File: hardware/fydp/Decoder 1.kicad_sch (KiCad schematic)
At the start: 21 parts, among them J2 Conn_01x02_Pin, J3 Conn_01x02_Pin, J6 Conn_01x04_Pin, U62 74HC139N

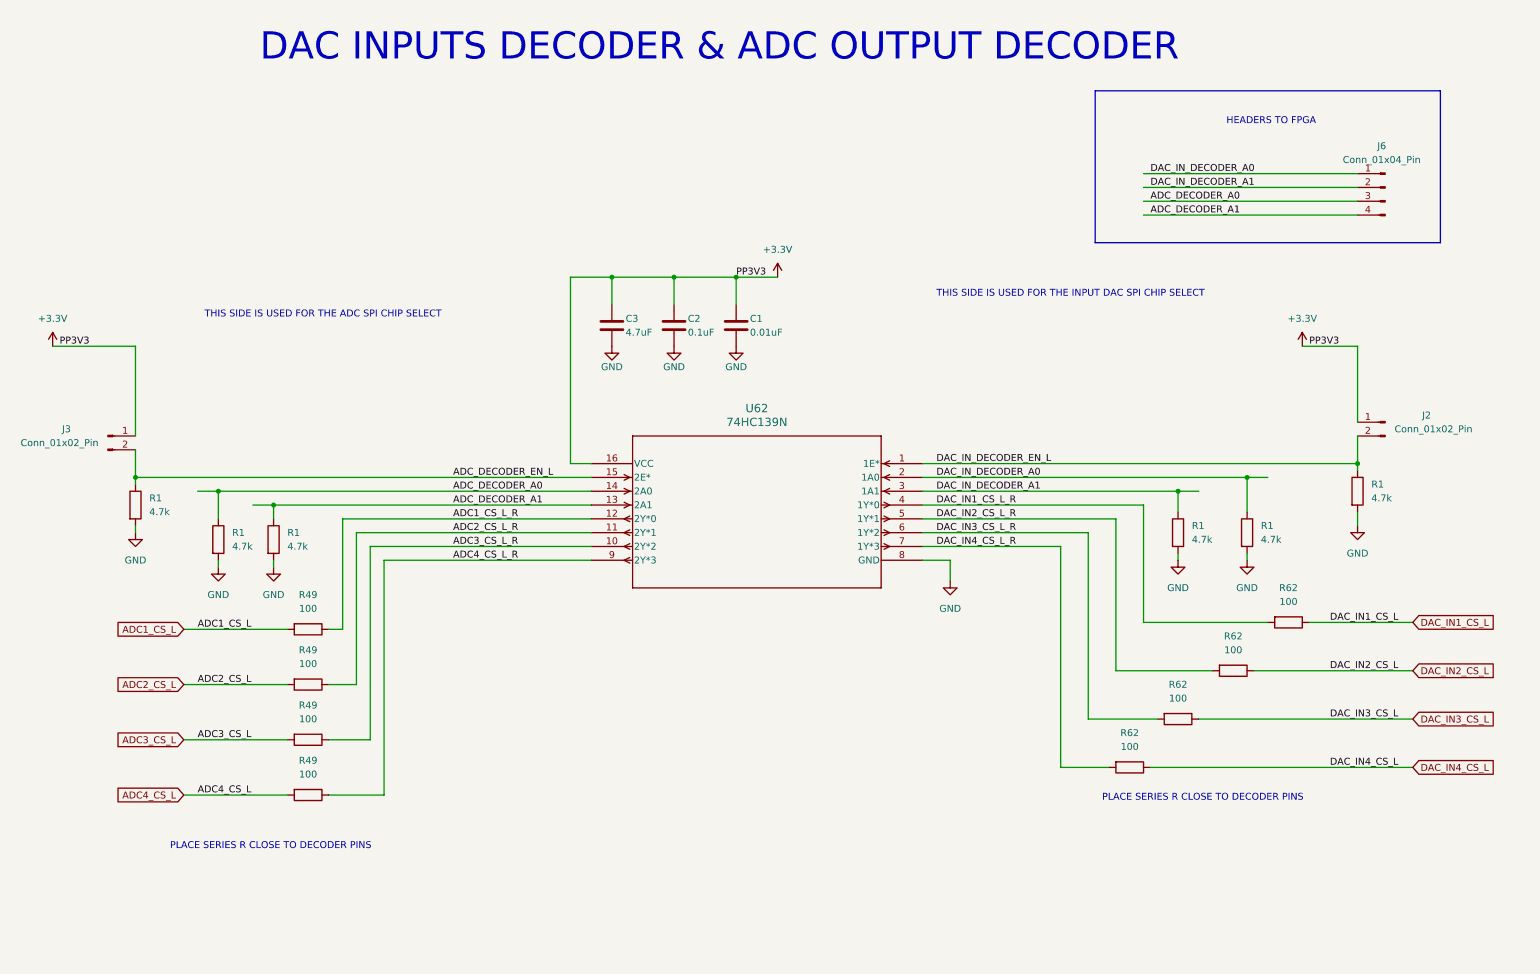
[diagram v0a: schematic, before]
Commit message: Remove 2 channels of multiplier and change ADC
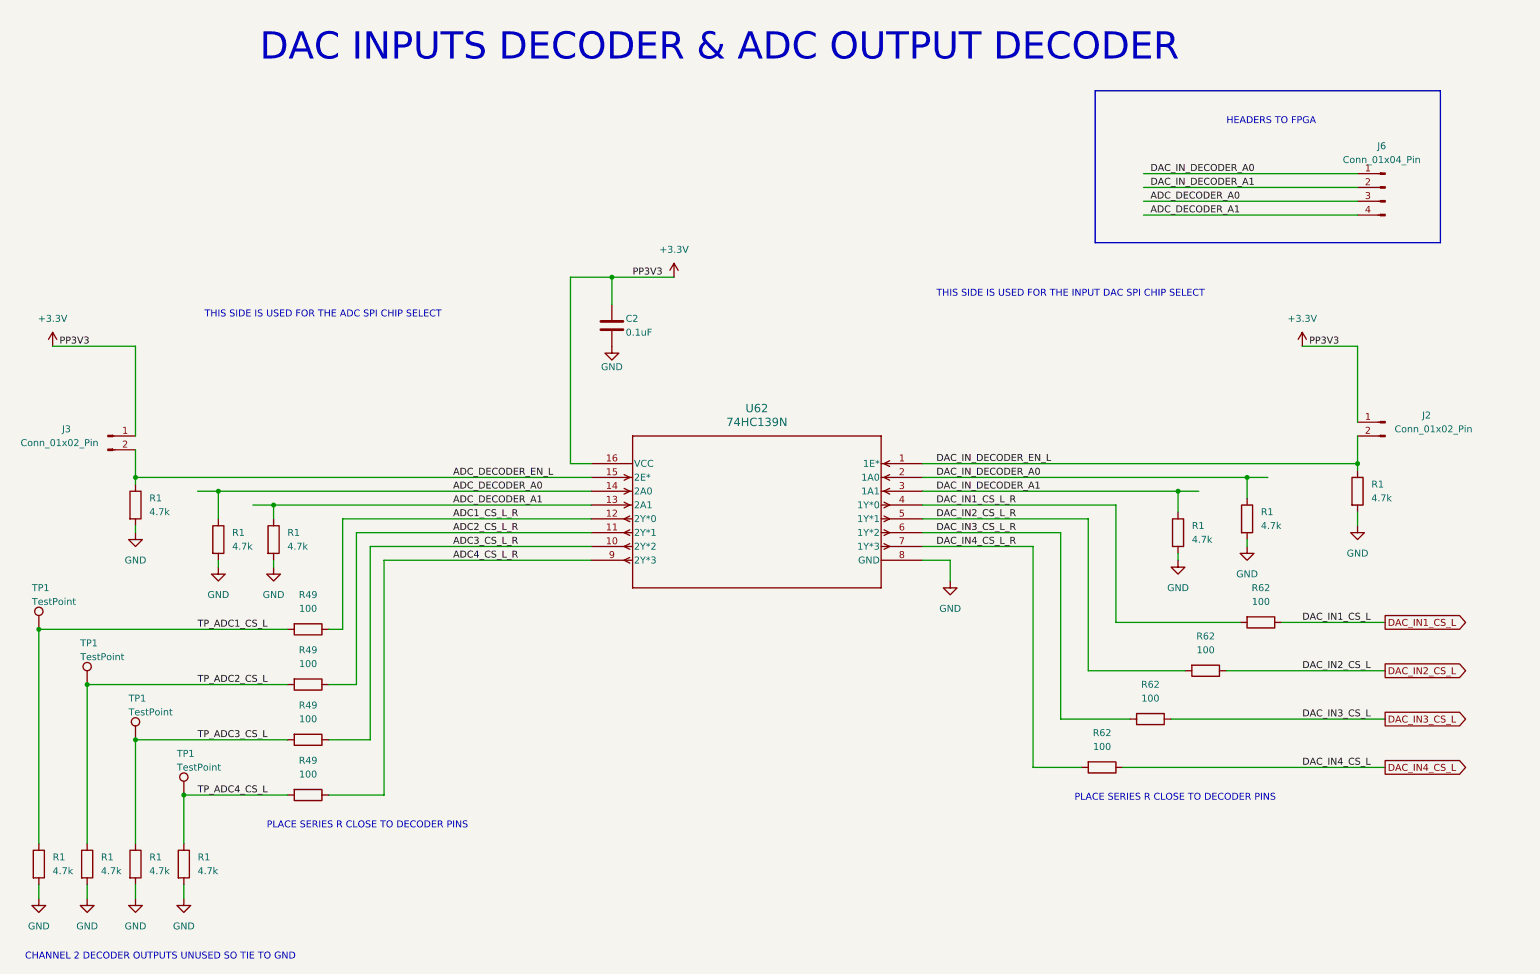
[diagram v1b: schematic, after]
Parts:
- removed C1: 0.01uF, Capacitor_SMD:C_0805_2012Metric, symbol Device:C
- removed C3: 4.7uF, Capacitor_SMD:C_0805_2012Metric, symbol Device:C
- added R1 (x4): 4.7k, Resistor_SMD:R_0805_2012Metric, symbol Device:R
- added TP1 (x4): TestPoint, TestPoint:TestPoint_Pad_1.0x1.0mm, symbol Connector:TestPoint
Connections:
- net GND: now also R1.2, R1.2, R1.2, R1.2
- net ADC1_CS_L renamed TP_ADC1_CS_L
- net TP_ADC1_CS_L: now also R1.1, TP1.1
- net ADC2_CS_L renamed TP_ADC2_CS_L
- net TP_ADC2_CS_L: now also R1.1, TP1.1
- net ADC3_CS_L renamed TP_ADC3_CS_L
- net TP_ADC3_CS_L: now also R1.1, TP1.1
- net ADC4_CS_L renamed TP_ADC4_CS_L
- net TP_ADC4_CS_L: now also R1.1, TP1.1
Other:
- note added: "CHANNEL 2 DECODER OUTPUTS UNUSED SO TIE TO GND"
- moved on the sheet: C2, R1, R62

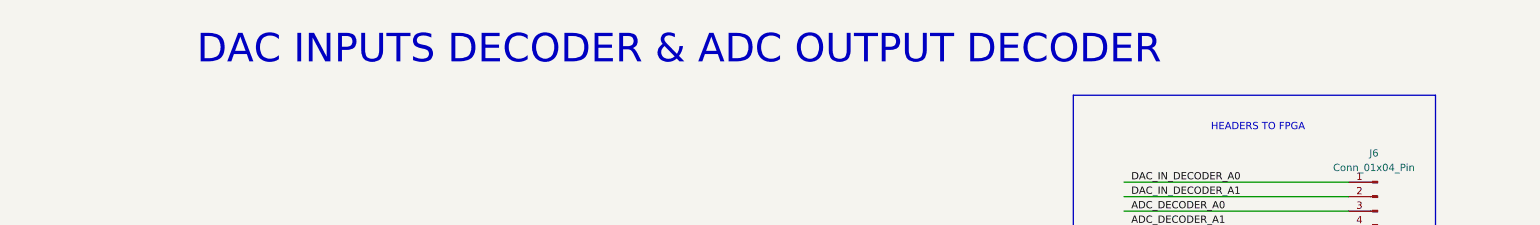
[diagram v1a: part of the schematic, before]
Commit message: Edit schematic titles
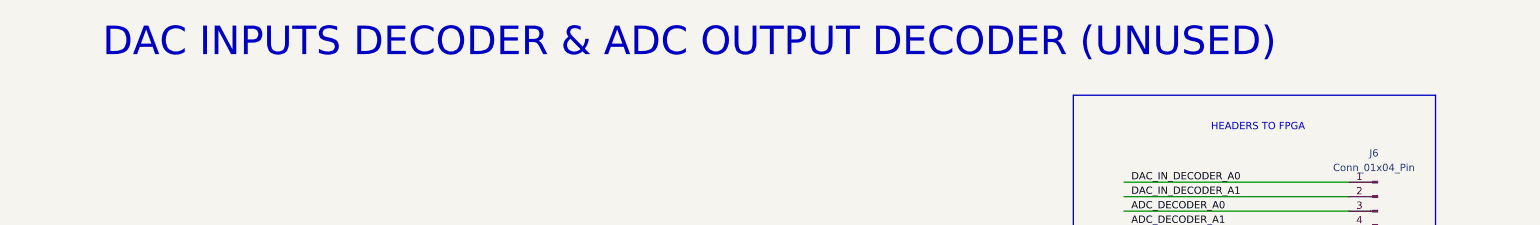
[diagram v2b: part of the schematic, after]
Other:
- note added: "DAC INPUTS DECODER & ADC OUTPUT DECODER (UNUSED)"
- note removed: "DAC INPUTS DECODER & ADC OUTPUT DECODER"
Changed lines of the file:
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@@
     (effects (font (size 1.27 1.27)) (justify left bottom))
   )
-  (text "DAC INPUTS DECODER & ADC OUTPUT DECODER" (at 59.69 26.67 0)
+  (text "DAC INPUTS DECODER & ADC OUTPUT DECODER (UNUSED)" (at 43.18 25.4 0)
     (effects (font (size 5 5)) (justify left bottom))
   )

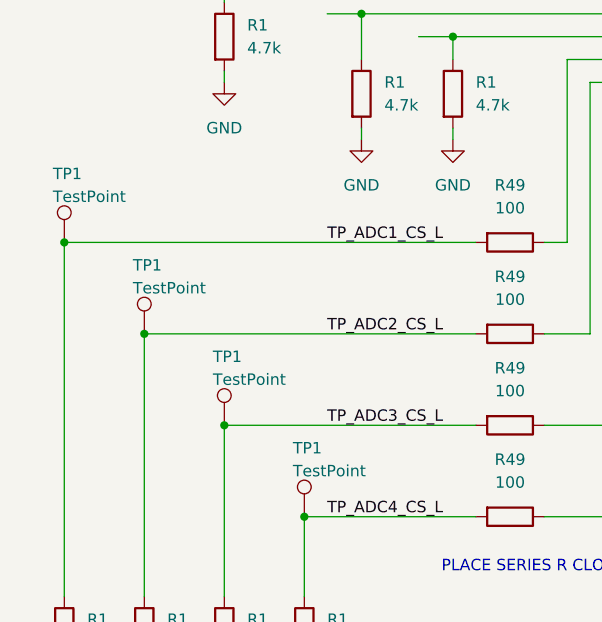
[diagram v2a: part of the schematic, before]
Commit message: Initial layout mostly complete, need to complete lots of routing
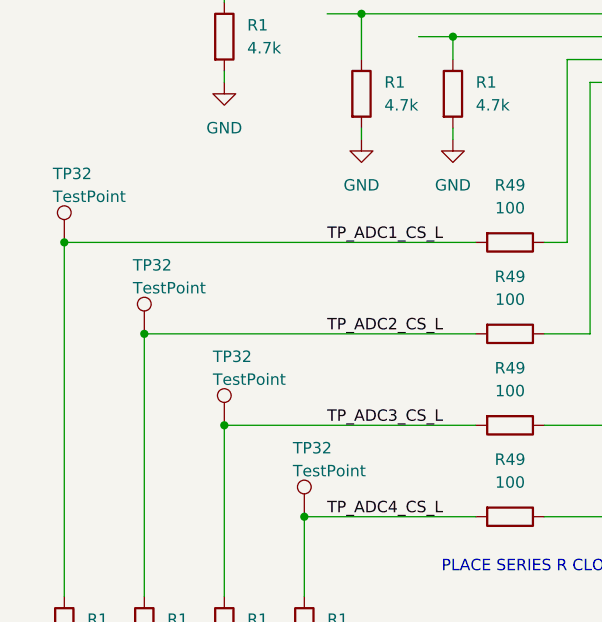
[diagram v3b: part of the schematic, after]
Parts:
- renumbered TP1 to TP32
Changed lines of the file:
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@@
   (symbol (lib_id "Connector:TestPoint") (at 27.94 140.97 0) (unit 1)
     (in_bom yes) (on_board yes) (dnp no)
-    (property "Reference" "TP1" (at 26.67 133.35 0)
+    (property "Reference" "TP32" (at 26.67 133.35 0)
       (effects (font (size 1.27 1.27)) (justify left))
     )
@@
   (symbol (lib_id "Connector:TestPoint") (at 36.83 151.13 0) (unit 1)
     (in_bom yes) (on_board yes) (dnp no)
-    (property "Reference" "TP1" (at 35.56 143.51 0)
+    (property "Reference" "TP32" (at 35.56 143.51 0)
       (effects (font (size 1.27 1.27)) (justify left))
     )
@@
   (symbol (lib_id "Connector:TestPoint") (at 45.72 161.29 0) (unit 1)
     (in_bom yes) (on_board yes) (dnp no)
-    (property "Reference" "TP1" (at 44.45 153.67 0)
+    (property "Reference" "TP32" (at 44.45 153.67 0)
       (effects (font (size 1.27 1.27)) (justify left))
     )
@@
   (symbol (lib_id "Connector:TestPoint") (at 19.05 130.81 0) (unit 1)
     (in_bom yes) (on_board yes) (dnp no)
-    (property "Reference" "TP1" (at 17.78 123.19 0)
-      (effects (font (size 1.27 1.27)) (justify left))
-    )
+    (property "Reference" "TP32" (at 17.78 123.19 0)
+      (effects (font (size 1.27 1.27)) (justify left))
+    )

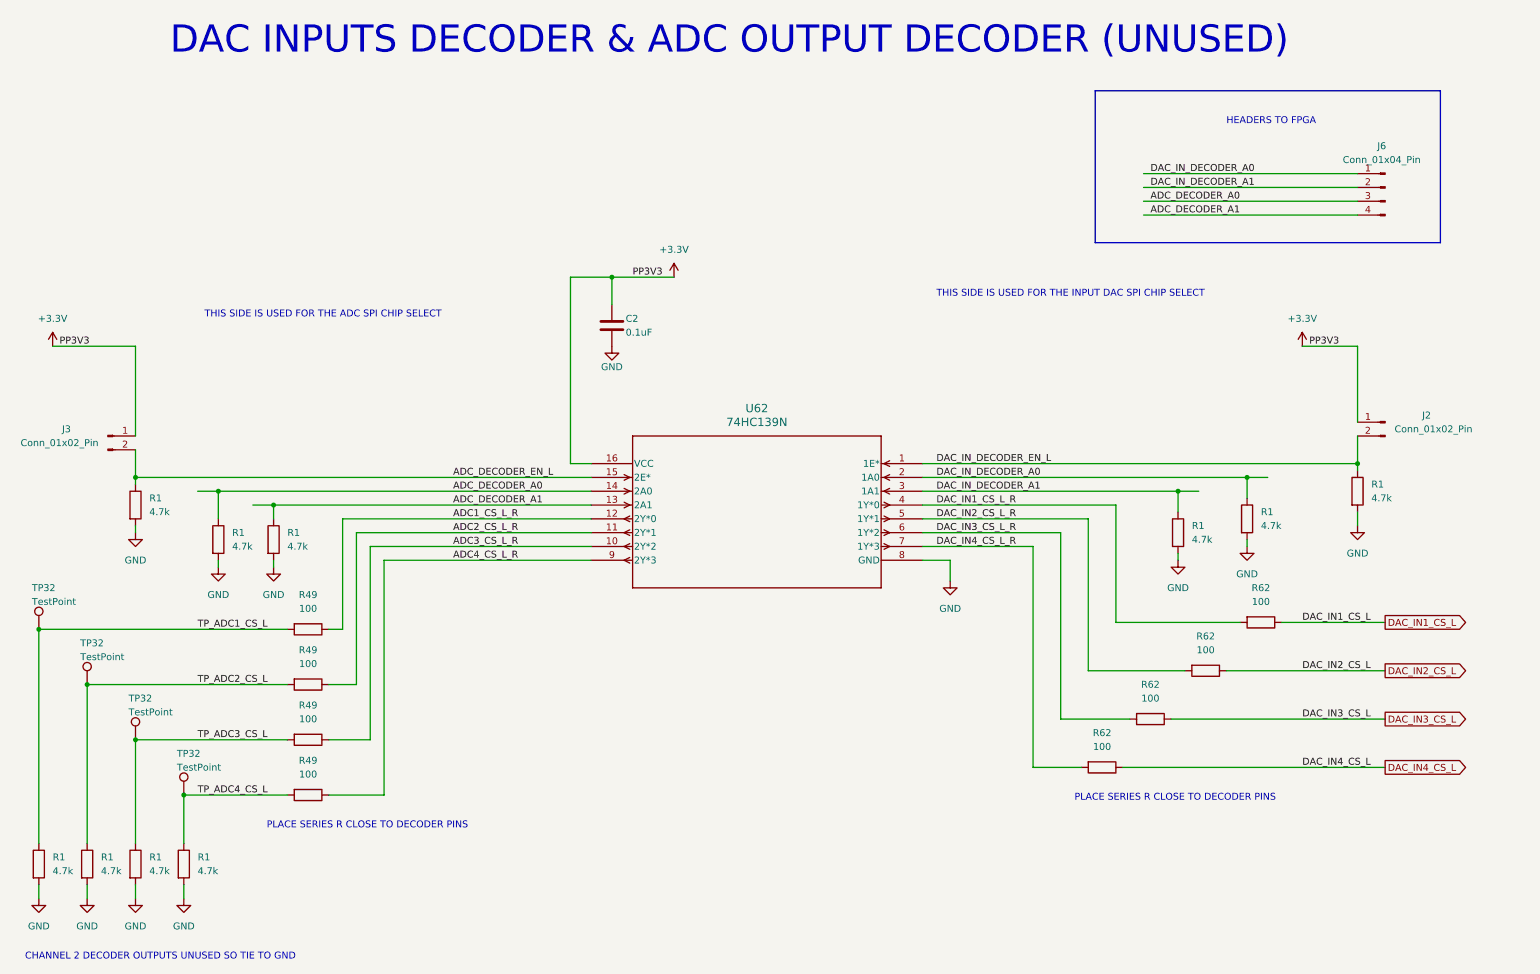
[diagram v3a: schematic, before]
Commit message: Completed placement and silk for left and centre sections of the PCB
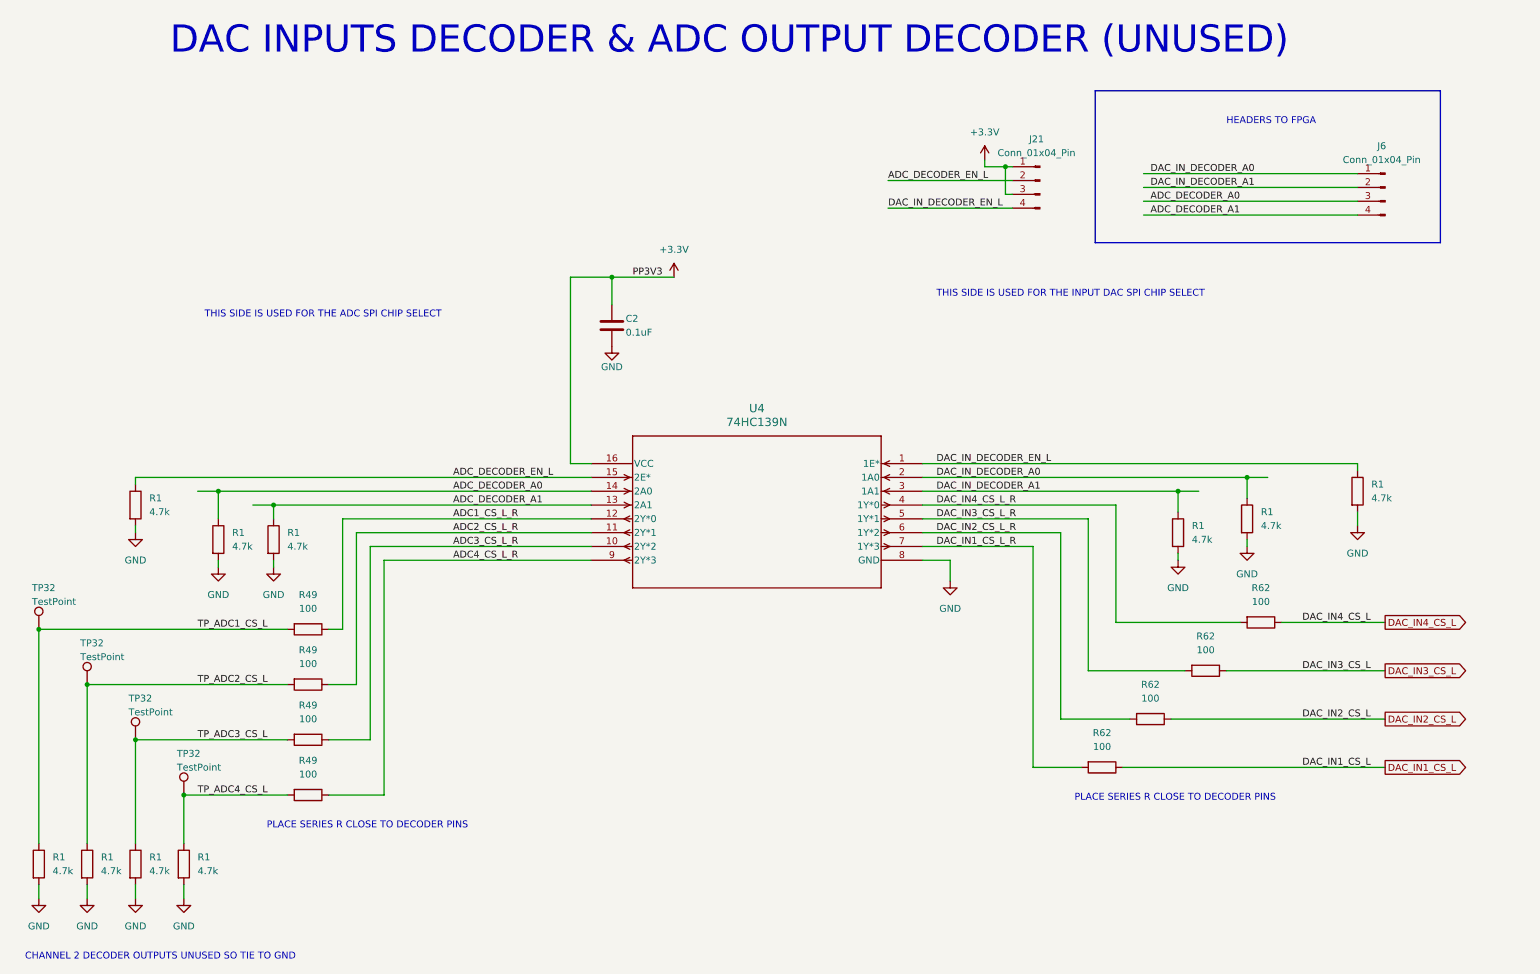
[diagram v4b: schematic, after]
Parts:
- removed J2, J3: Conn_01x02_Pin, Connector_PinHeader_2.54mm:PinHeader_1x02_P2.54mm_Vertical, symbol Connector:Conn_01x02_Pin
- added J21: Conn_01x04_Pin, Connector_PinHeader_2.54mm:PinHeader_1x04_P2.54mm_Vertical, symbol Connector:Conn_01x04_Pin
- renumbered U62 to U4
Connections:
- net +3.3V: now also J21.1 (Pin_1), J21.3 (Pin_3)
- net ADC_DECODER_EN_L: now also J21.2 (Pin_2)
- net DAC_IN1_CS_L: now also R62.1; no longer R62.1
- net DAC_IN1_CS_L_R: now also R62.2, U4.7 (1Y*3); no longer R62.2, U4.4 (1Y*0)
- net DAC_IN2_CS_L: now also R62.1; no longer R62.1
- net DAC_IN2_CS_L_R: now also R62.2, U4.6 (1Y*2); no longer R62.2, U4.5 (1Y*1)
- net DAC_IN3_CS_L: now also R62.1; no longer R62.1
- net DAC_IN3_CS_L_R: now also R62.2, U4.5 (1Y*1); no longer R62.2, U4.6 (1Y*2)
- net DAC_IN4_CS_L: now also R62.1; no longer R62.1
- net DAC_IN4_CS_L_R: now also R62.2, U4.4 (1Y*0); no longer R62.2, U4.7 (1Y*3)
- net DAC_IN_DECODER_EN_L: now also J21.4 (Pin_4)
